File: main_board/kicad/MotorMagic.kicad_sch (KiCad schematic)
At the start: 0 parts

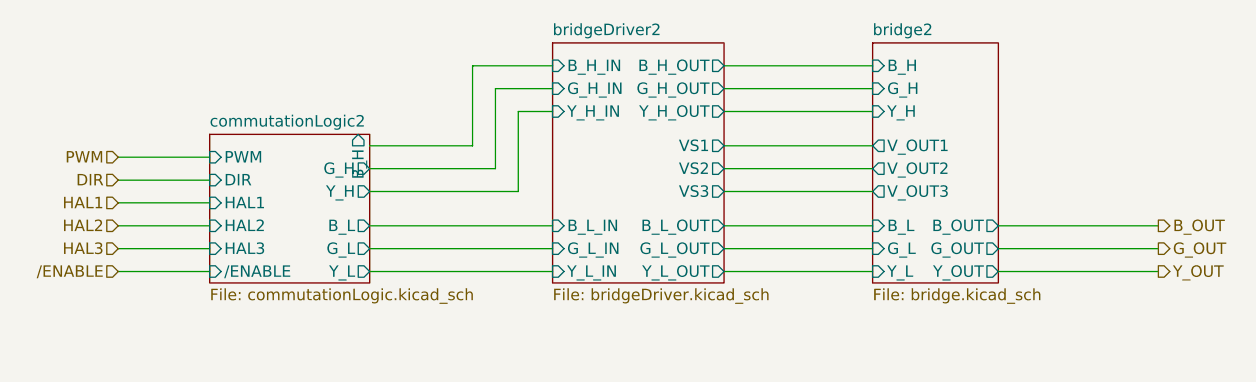
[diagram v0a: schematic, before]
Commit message: resolved ERC
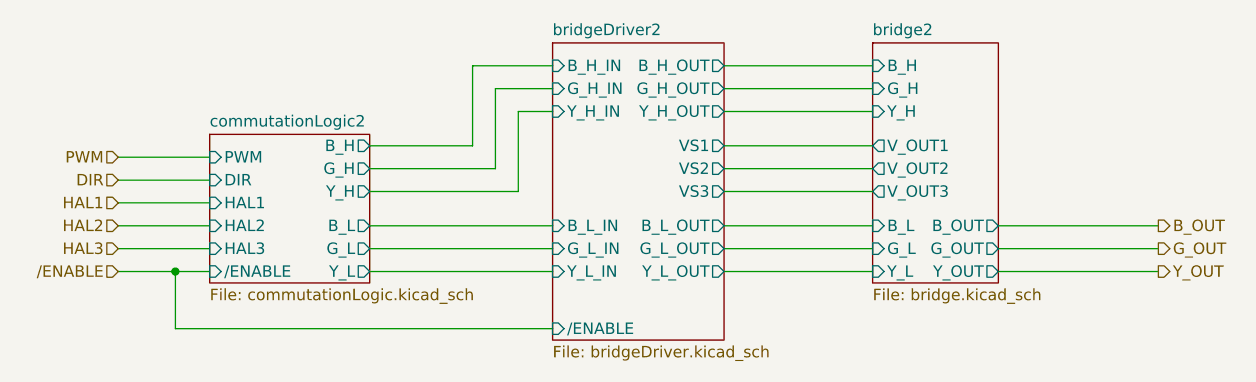
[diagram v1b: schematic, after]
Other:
- sheet bridgeDriver2 ports: added /ENABLE; removed none
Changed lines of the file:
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@@
 (kicad_sch (version 20230121) (generator eeschema)
   (paper "A4")
+  (junction (at 64.77 99.06) (diameter 0) (color 0 0 0 0)
+  )
   (wire (pts (xy 125.73 99.06) (xy 142.24 99.06))
     (stroke (width 0) (type default))
   )
+  (wire (pts (xy 64.77 105.41) (xy 64.77 99.06))
+    (stroke (width 0) (type default))
+  )
   (wire (pts (xy 156.21 99.06) (xy 173.99 99.06))
     (stroke (width 0) (type default))
@@
     (stroke (width 0) (type default))
   )
-  (wire (pts (xy 58.42 99.06) (xy 68.58 99.06))
+  (wire (pts (xy 58.42 99.06) (xy 64.77 99.06))
     (stroke (width 0) (type default))
   )
@@
     (stroke (width 0) (type default))
   )
+  (wire (pts (xy 106.68 105.41) (xy 64.77 105.41))
+    (stroke (width 0) (type default))
+  )
   (wire (pts (xy 58.42 96.52) (xy 68.58 96.52))
     (stroke (width 0) (type default))
@@
   )
   (wire (pts (xy 102.87 81.28) (xy 106.68 81.28))
+    (stroke (width 0) (type default))
+  )
+  (wire (pts (xy 64.77 99.06) (xy 68.58 99.06))
     (stroke (width 0) (type default))
   )
@@
       (effects (font (size 1.27 1.27)) (justify left))
     )
-    (pin "B_H" output (at 85.09 83.82 90)
+    (pin "B_H" output (at 86.36 85.09 0)
       (effects (font (size 1.27 1.27)) (justify right))
     )
@@
     )
   )
-  (sheet (at 106.68 73.66) (size 19.05 26.67) (fields_autoplaced)
+  (sheet (at 106.68 73.66) (size 19.05 33.02) (fields_autoplaced)
     (stroke (width 0.1524) (type solid))
     (fill (color 0 0 0 0.0000))
@@
       (effects (font (size 1.27 1.27)) (justify left bottom))
     )
-    (property "Sheetfile" "bridgeDriver.kicad_sch" (at 106.68 100.9146 0)
+    (property "Sheetfile" "bridgeDriver.kicad_sch" (at 106.68 107.2646 0)
       (effects (font (size 1.27 1.27)) (justify left top))
     )
@@
       (effects (font (size 1.27 1.27)) (justify right))
     )
+    (pin "{slash}ENABLE" input (at 106.68 105.41 180)
+      (effects (font (size 1.27 1.27)) (justify left))
+    )
     (instances

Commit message: updated to post review state
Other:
- sheet commutationLogic2 ports: added none; removed /ENABLE
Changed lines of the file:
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@@
 (kicad_sch (version 20230121) (generator eeschema)
   (paper "A4")
-  (junction (at 64.77 99.06) (diameter 0) (color 0 0 0 0)
-  )
   (wire (pts (xy 125.73 99.06) (xy 142.24 99.06))
-    (stroke (width 0) (type default))
-  )
-  (wire (pts (xy 64.77 105.41) (xy 64.77 99.06))
     (stroke (width 0) (type default))
   )
@@
     (stroke (width 0) (type default))
   )
-  (wire (pts (xy 58.42 99.06) (xy 64.77 99.06))
-    (stroke (width 0) (type default))
-  )
   (wire (pts (xy 125.73 76.2) (xy 142.24 76.2))
     (stroke (width 0) (type default))
@@
     (stroke (width 0) (type default))
   )
-  (wire (pts (xy 106.68 105.41) (xy 64.77 105.41))
+  (wire (pts (xy 58.42 105.41) (xy 106.68 105.41))
     (stroke (width 0) (type default))
   )
@@
   )
   (wire (pts (xy 102.87 81.28) (xy 106.68 81.28))
-    (stroke (width 0) (type default))
-  )
-  (wire (pts (xy 64.77 99.06) (xy 68.58 99.06))
     (stroke (width 0) (type default))
   )
@@
     (effects (font (size 1.27 1.27)) (justify right))
   )
-  (hierarchical_label "{slash}ENABLE" (shape input) (at 58.42 99.06 180) (fields_autoplaced)
+  (hierarchical_label "{slash}ENABLE" (shape input) (at 58.42 105.41 180) (fields_autoplaced)
     (effects (font (size 1.27 1.27)) (justify right))
   )
@@
       (effects (font (size 1.27 1.27)) (justify left))
     )
-    (pin "{slash}ENABLE" input (at 68.58 99.06 180)
-      (effects (font (size 1.27 1.27)) (justify left))
-    )
